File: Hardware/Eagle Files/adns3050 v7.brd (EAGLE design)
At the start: 30.5 x 51.9 mm, 7 parts, among them U1 V_REG_317SMD

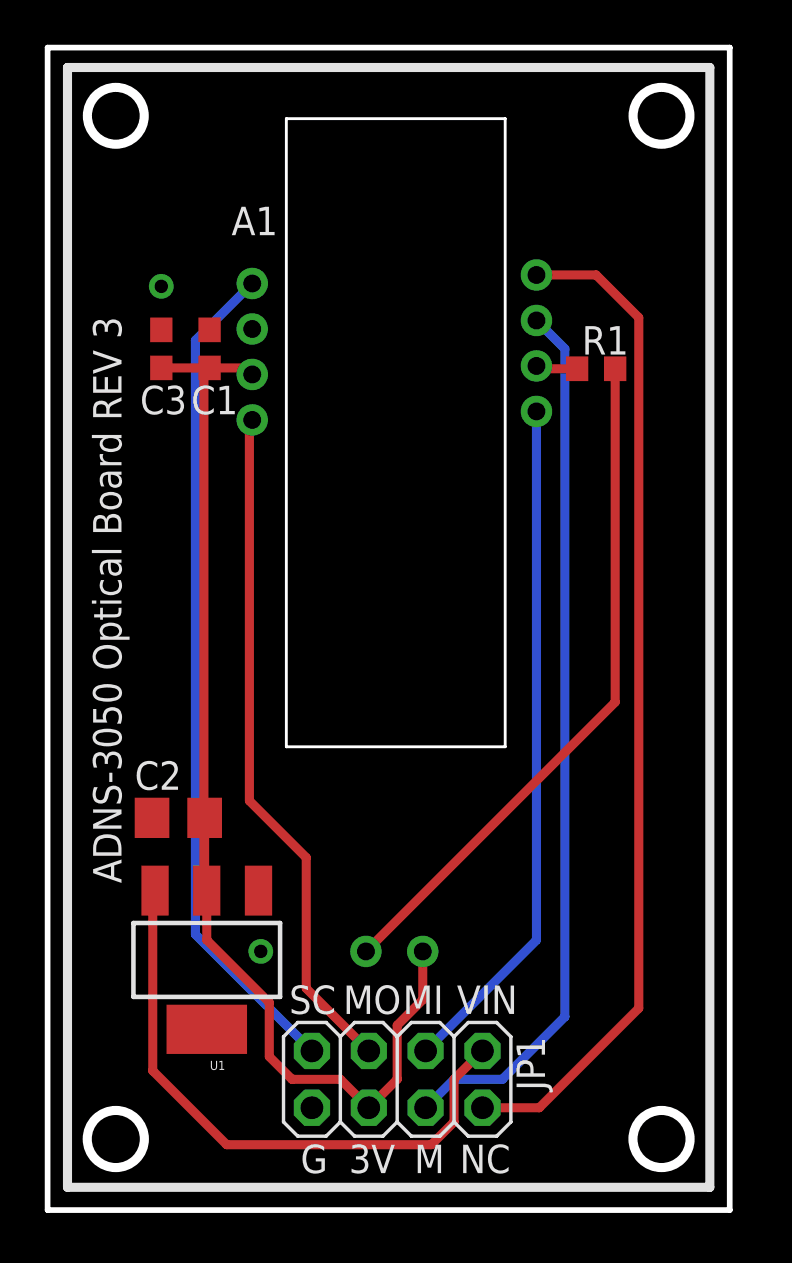
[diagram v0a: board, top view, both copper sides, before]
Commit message: Updated board, increased text spacing
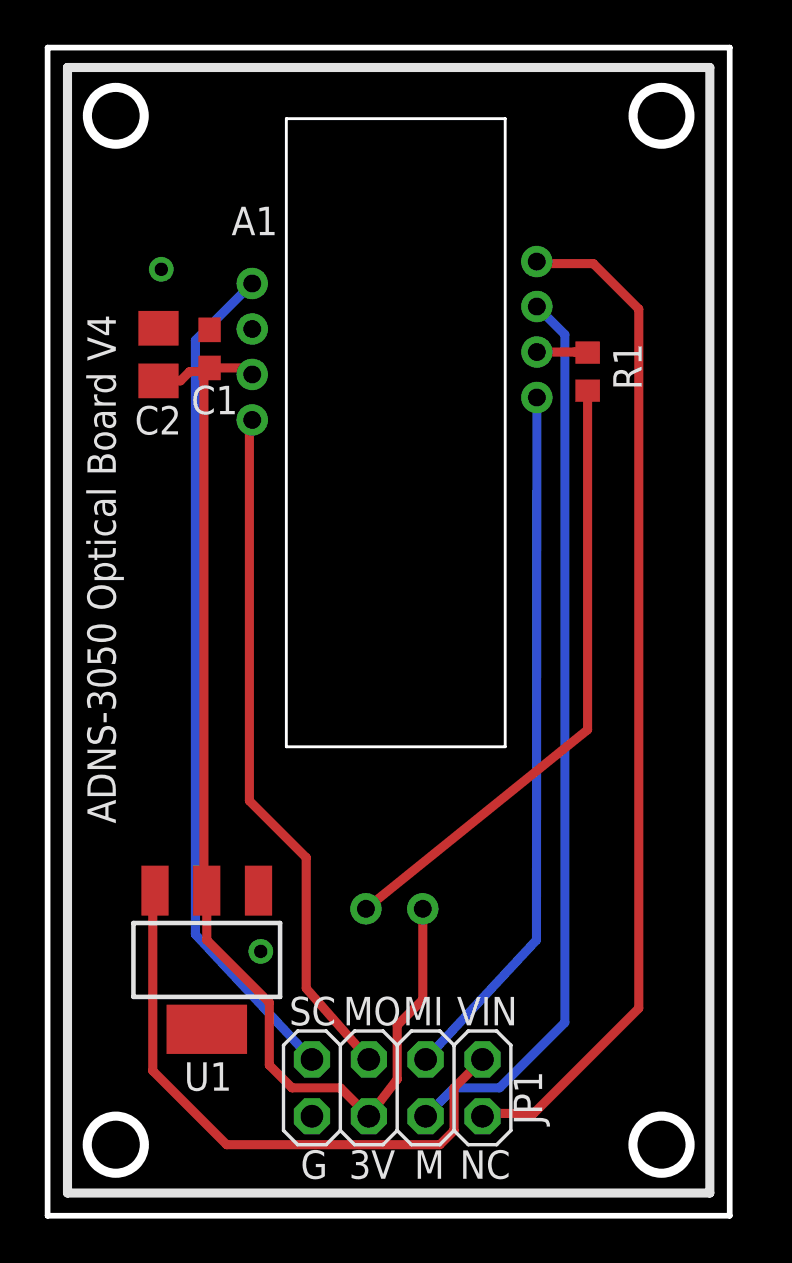
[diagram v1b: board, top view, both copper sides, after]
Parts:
- removed C3: (no value), eagle-ltspice:C0603
- moved C2 20.7 mm to (6.99, 30.4), turned to 270 degrees
- moved R1 0.40 mm to (26.2, 29.6), turned to 270 degrees
- moved JP1 0.38 mm to (17.7, -2.41)
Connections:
- net GND: no longer C3.2
- net VDD: no longer C3.1
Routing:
- net N$3: track 30.6 -> 27.9 mm
- net MOTION: track 39.5 -> 40.5 mm
- net MISO: track 30.6 -> 31.5 mm
- net NCS: track 45.0 -> 45.7 mm
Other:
- board size 30.5 x 51.9 mm -> 30.5 x 52.2 mm
- board text added: "ADNS-3050 Optical Board V4"
- board text added: "U1"
- board text removed: "ADNS-3050 Optical Board REV 3"

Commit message: Updated Gerbers + Documentation
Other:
- board size 30.5 x 52.2 mm -> 31.1 x 52.2 mm
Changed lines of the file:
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@@
 <board>
 <plain>
-<wire x1="32.512" y1="44.069" x2="32.512" y2="-8.128" width="0.254" layer="20"/>
+<wire x1="33.147" y1="44.069" x2="33.147" y2="-8.128" width="0.254" layer="20"/>
 <wire x1="2.032" y1="44.069" x2="2.032" y2="-8.128" width="0.254" layer="20"/>
-<wire x1="32.512" y1="44.069" x2="2.032" y2="44.069" width="0.254" layer="20"/>
-<wire x1="32.512" y1="-8.128" x2="2.032" y2="-8.128" width="0.254" layer="20"/>
+<wire x1="33.147" y1="44.069" x2="2.032" y2="44.069" width="0.254" layer="20"/>
+<wire x1="33.147" y1="-8.128" x2="2.032" y2="-8.128" width="0.254" layer="20"/>
 <circle x="5.08" y="41.021" radius="1.27" width="0.4064" layer="20"/>
-<circle x="29.464" y="41.021" radius="1.27" width="0.4064" layer="20"/>
+<circle x="30.099" y="41.021" radius="1.27" width="0.4064" layer="20"/>
 <circle x="5.08" y="-4.953" radius="1.27633125" width="0.4064" layer="20"/>
-<circle x="29.464" y="-4.953" radius="1.27633125" width="0.4064" layer="20"/>
+<circle x="30.099" y="-4.953" radius="1.27633125" width="0.4064" layer="20"/>
 <wire x1="2.921" y1="43.18" x2="2.921" y2="-7.112" width="0.4064" layer="21"/>
-<wire x1="2.921" y1="-7.112" x2="31.623" y2="-7.112" width="0.4064" layer="21"/>
-<wire x1="31.623" y1="-7.112" x2="31.623" y2="43.18" width="0.4064" layer="21"/>
-<wire x1="31.623" y1="43.18" x2="2.921" y2="43.18" width="0.4064" layer="21"/>
+<wire x1="2.921" y1="-7.112" x2="32.258" y2="-7.112" width="0.4064" layer="21"/>
+<wire x1="32.258" y1="-7.112" x2="32.258" y2="43.18" width="0.4064" layer="21"/>
+<wire x1="32.258" y1="43.18" x2="2.921" y2="43.18" width="0.4064" layer="21"/>
 <text x="12.827" y="0.381" size="1.27" layer="21">SC</text>
 <text x="15.24" y="0.381" size="1.27" layer="21">MO</text>
@@
 <vertex x="2.032" y="-8.128"/>
 <vertex x="2.032" y="44.069"/>
-<vertex x="32.512" y="44.069"/>
-<vertex x="32.512" y="-8.128"/>
+<vertex x="33.147" y="44.069"/>
+<vertex x="33.147" y="-8.128"/>
 </polygon>
 <polygon width="0.254" layer="1" isolate="0.3048">
 <vertex x="2.032" y="-8.128"/>
 <vertex x="2.032" y="44.069"/>
-<vertex x="32.512" y="44.069"/>
-<vertex x="32.512" y="-8.128"/>
+<vertex x="33.147" y="44.069"/>
+<vertex x="33.147" y="-8.128"/>
 </polygon>
 <contactref element="C1" pad="2"/>
